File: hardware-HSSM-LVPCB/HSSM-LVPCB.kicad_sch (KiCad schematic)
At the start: 57 parts, among them J1 UFL_R_SMT_1_10, J2 LPPB061NGCN-RC, Q1 Q_MOSFET_N_BSS123, Q2 Q_MOSFET_N_BSS123, U1 ESP32-C6, U2 W25Q64JVSSIQ_SOIC-8, X1 X_40MHz_SMD_ECS-2520SMV-400-F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

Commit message: [#13] PCB routing WIP GPIO
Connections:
- net GPIO_Q2: now also U1.16 (GPIO10); no longer U1.6 (XTAL_32K_P)
- net GPIO_S2: now also U1.18 (GPIO12); no longer U1.17 (GPIO11)
- net GPIO_S3: now also U1.17 (GPIO11)
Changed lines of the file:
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@@
-	(wire
-		(pts
-			(xy 93.98 121.92) (xy 104.14 121.92)
-		)
-		(stroke
-			(width 0)
-			(type default)
-		)
-	)
 	(wire
 		(pts
@@
 	(wire
 		(pts
+			(xy 152.4 165.1) (xy 152.4 154.94)
+		)
+		(stroke
+			(width 0)
+			(type default)
+		)
+	)
+	(wire
+		(pts
 			(xy 193.04 54.61) (xy 191.77 54.61)
 		)
@@
 	(wire
 		(pts
+			(xy 142.24 165.1) (xy 142.24 154.94)
+		)
+		(stroke
+			(width 0)
+			(type default)
+		)
+	)
+	(wire
+		(pts
 			(xy 180.34 50.8) (xy 193.04 50.8)
 		)
@@
 	(wire
 		(pts
+			(xy 147.32 165.1) (xy 147.32 154.94)
+		)
+		(stroke
+			(width 0)
+			(type default)
+		)
+	)
+	(wire
+		(pts
 			(xy 152.4 83.82) (xy 152.4 77.47)
 		)
@@
 		(pts
 			(xy 280.67 219.71) (xy 290.83 219.71)
-		)
-		(stroke
-			(width 0)
-			(type default)
-		)
-	)
-	(wire
-		(pts
-			(xy 147.32 165.1) (xy 147.32 154.94)
 		)
 		(stroke
@@
 		)
 	)
-	(label "GPIO_S2"
-		(at 147.32 165.1 90)
-		(fields_autoplaced yes)
-		(effects
-			(font
-				(size 1.27 1.27)
-			)
-			(justify left bottom)
-		)
-	)
 	(label "GPIO_S3"
 		(at 187.96 68.58 0)
@@
 		)
 	)
-	(label "GPIO_Q2"
-		(at 93.98 121.92 0)
-		(fields_autoplaced yes)
-		(effects
-			(font
-				(size 1.27 1.27)
-			)
-			(justify left bottom)
-		)
-	)
 	(label "GPIO_Q1"
 		(at 162.56 73.66 270)
@@
 		)
 	)
+	(label "GPIO_S3"
+		(at 147.32 165.1 90)
+		(fields_autoplaced yes)
+		(effects
+			(font
+				(size 1.27 1.27)
+			)
+			(justify left bottom)
+		)
+	)
 	(label "S3_sym"
 		(at 95.25 132.08 0)
@@
 		)
 	)
+	(label "GPIO_Q2"
+		(at 142.24 165.1 90)
+		(fields_autoplaced yes)
+		(effects
+			(font
+				(size 1.27 1.27)
+			)
+			(justify left bottom)
+		)
+	)
 	(label "GPIO_S1"
 		(at 157.48 73.66 270)
@@
 		(fields_autoplaced yes)
 		(effects
+			(font
+				(size 1.27 1.27)
+			)
+			(justify left bottom)
+		)
+	)
+	(label "GPIO_S2"
+		(at 152.4 165.1 90)
+		(fields_autoplaced yes)
+		(effects

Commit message: Add additional signals to FCB between PCBs
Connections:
- net DEV_RX is gone; now on net LP_UART_TXD: CON1.8
- net DEV_TX is gone; now on net LP_UART_RXD: CON1.7
- net P_MEAS_RST: now reaches CON1.10
- net DO3: now reaches CON1.5
- net DO2: now reaches CON1.6
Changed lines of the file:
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@@
-	(wire
-		(pts
-			(xy 240.03 152.4) (xy 251.46 152.4)
-		)
-		(stroke
-			(width 0)
-			(type default)
-		)
-	)
 	(wire
 		(pts
@@
 	(wire
 		(pts
-			(xy 240.03 160.02) (xy 251.46 160.02)
+			(xy 228.6 160.02) (xy 251.46 160.02)
 		)
 		(stroke
@@
 	(wire
 		(pts
-			(xy 240.03 154.94) (xy 251.46 154.94)
-		)
-		(stroke
-			(width 0)
-			(type default)
-		)
-	)
-	(wire
-		(pts
-			(xy 240.03 147.32) (xy 251.46 147.32)
+			(xy 233.68 147.32) (xy 251.46 147.32)
 		)
 		(stroke
@@
 	(wire
 		(pts
-			(xy 187.96 73.66) (xy 198.12 73.66)
-		)
-		(stroke
-			(width 0)
-			(type default)
-		)
-	)
-	(wire
-		(pts
 			(xy 55.88 87.63) (xy 55.88 90.17)
 		)
@@
 	(wire
 		(pts
-			(xy 187.96 83.82) (xy 198.12 83.82)
-		)
-		(stroke
-			(width 0)
-			(type default)
-		)
-	)
-	(wire
-		(pts
 			(xy 128.27 176.53) (xy 132.08 176.53)
 		)
@@
 	(wire
 		(pts
-			(xy 187.96 68.58) (xy 198.12 68.58)
-		)
-		(stroke
-			(width 0)
-			(type default)
-		)
-	)
-	(wire
-		(pts
 			(xy 250.19 137.16) (xy 251.46 137.16)
 		)
@@
 	(wire
 		(pts
-			(xy 222.25 154.94) (xy 236.22 154.94)
+			(xy 237.49 152.4) (xy 251.46 152.4)
 		)
 		(stroke
@@
 	(wire
 		(pts
-			(xy 187.96 78.74) (xy 198.12 78.74)
-		)
-		(stroke
-			(width 0)
-			(type default)
-		)
-	)
-	(wire
-		(pts
 			(xy 271.78 219.71) (xy 280.67 219.71)
 		)
@@
 	(wire
 		(pts
-			(xy 240.03 149.86) (xy 251.46 149.86)
+			(xy 233.68 149.86) (xy 251.46 149.86)
 		)
 		(stroke
@@
 	(wire
 		(pts
+			(xy 146.05 177.8) (xy 168.91 177.8)
+		)
+		(stroke
+			(width 0)
+			(type default)
+		)
+	)
+	(wire
+		(pts
 			(xy 392.43 224.79) (xy 389.89 224.79)
 		)
@@
 	(wire
 		(pts
-			(xy 222.25 152.4) (xy 236.22 152.4)
+			(xy 237.49 154.94) (xy 251.46 154.94)
 		)
 		(stroke
@@
 		)
 	)
-	(label "GPIO23"
-		(at 187.96 83.82 0)
-		(fields_autoplaced yes)
-		(effects
-			(font
-				(size 1.27 1.27)
-			)
-			(justify left bottom)
-		)
-	)
 	(label "GPIO8"
 		(at 132.08 165.1 90)
@@
 		)
 	)
-	(label "DEV_TX"
-		(at 240.03 152.4 0)
-		(fields_autoplaced yes)
-		(effects
-			(font
-				(size 1.27 1.27)
-			)
-			(justify left bottom)
-		)
-	)
 	(label "S2_sym"
 		(at 93.98 127 0)
@@
 		)
 	)
+	(label "DO3"
+		(at 233.68 147.32 0)
+		(fields_autoplaced yes)
+		(effects
+			(font
+				(size 1.27 1.27)
+			)
+			(justify left bottom)
+		)
+	)
 	(label "SPICLK"
 		(at 204.47 121.92 180)
@@
 		)
 	)
-	(label "GPIO_S3"
-		(at 187.96 68.58 0)
-		(fields_autoplaced yes)
-		(effects
-			(font
-				(size 1.27 1.27)
-			)
-			(justify left bottom)
-		)
-	)
 	(label "LP_UART_TXD"
 		(at 116.84 168.91 90)
@@
 		)
 	)
+	(label "DO2"
+		(at 233.68 149.86 0)
+		(fields_autoplaced yes)
+		(effects
+			(font
+				(size 1.27 1.27)
+			)
+			(justify left bottom)
+		)
+	)
 	(label "SPIWP"
 		(at 204.47 137.16 180)
@@
 		)
 	)
-	(label "GPIO22"
-		(at 187.96 78.74 0)
-		(fields_autoplaced yes)
-		(effects
-			(font
-				(size 1.27 1.27)
-			)
-			(justify left bottom)
-		)
-	)
-	(label "DEV_RX"
-		(at 240.03 154.94 0)
+	(label "P_MEAS_RST"
+		(at 146.05 177.8 0)
 		(fields_autoplaced yes)
 		(effects
@@
 		)
 	)
-	(label "GPIO21"
-		(at 187.96 73.66 0)
-		(fields_autoplaced yes)
-		(effects
-			(font
-				(size 1.27 1.27)
-			)
-			(justify left bottom)
-		)
-	)
 	(label "LP_UART_RXD"
-		(at 222.25 154.94 0)
+		(at 237.49 152.4 0)
 		(fields_autoplaced yes)
 		(effects
@@
 		)
 	)
+	(label "P_MEAS_RST"
+		(at 228.6 160.02 0)
+		(fields_autoplaced yes)
+		(effects
+			(font
+				(size 1.27 1.27)
+			)
+			(justify left bottom)
+		)
+	)
 	(label "SPICLK"
 		(at 231.14 50.8 180)
@@
 	)
 	(label "LP_UART_TXD"
-		(at 222.25 152.4 0)
-		(fields_autoplaced yes)
-		(effects
+		(at 237.49 154.94 0)
+		(fields_autoplaced yes)
+		(effects

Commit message: [#13] PCB routing WIP prog signals
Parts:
- removed Q1, Q2: Q_MOSFET_N_BSS123, HSSM-LVPCB:SOT-23, symbol HSSM-LVPCB:Q_MOSFET_N_BSS123
- removed R10, R9: R_499R_1pct_0402_RC0402FR-07499RL, HSSM-LVPCB:R_0402, symbol HSSM-LVPCB:R_499R_1pct_0402_RC0402FR-07499RL
- removed R20, R21: R_10k_1pct_0402_RC0402FR-0710KL, HSSM-LVPCB:R_0402, symbol HSSM-LVPCB:R_10k_1pct_0402_RC0402FR-0710KL
- added C15, C20, C21: C_0u1_10pct_50V_0402_GRM155R71H104KE14D, HSSM-LVPCB:C_0402, symbol HSSM-LVPCB:C_0u1_10pct_50V_0402_GRM155R71H104KE14D
- added R23, R24: R_10k_1pct_0402_RC0402FR-0710KL, HSSM-LVPCB:R_0402, symbol HSSM-LVPCB:R_10k_1pct_0402_RC0402FR-0710KL
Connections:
- net DTR is gone; now on net BOOT: J2.2
- net RTS is gone; now on net Enable: J2.3
- net +3V3: now also R23.1, R24.1
- net BOOT: now also C20.2, R23.2
- net Enable: now also C15.2, R24.2
- net GND: now also C15.1, C20.1, C21.1
- net GPIO8: now also C21.2
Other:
- moved on the sheet: J2, R22

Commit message: [#13] PCB routing WIP GPIO
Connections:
- net S3_sym: now also U1.12 (MTCK); no longer U1.8 (GPIO2)
- no-connect marks 3 -> 2
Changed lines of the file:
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@@
 		(at 127 154.94)
 	)
-	(no_connect
-		(at 121.92 154.94)
-	)
 	(wire
 		(pts
@@
 	(wire
 		(pts
+			(xy 121.92 163.83) (xy 121.92 154.94)
+		)
+		(stroke
+			(width 0)
+			(type default)
+		)
+	)
+	(wire
+		(pts
 			(xy 336.55 212.09) (xy 336.55 217.17)
 		)
@@
 		(pts
 			(xy 351.79 217.17) (xy 351.79 212.09)
-		)
-		(stroke
-			(width 0)
-			(type default)
-		)
-	)
-	(wire
-		(pts
-			(xy 95.25 132.08) (xy 104.14 132.08)
 		)
 		(stroke
@@
 		)
 	)
+	(label "S3_sym"
+		(at 121.92 163.83 90)
+		(fields_autoplaced yes)
+		(effects
+			(font
+				(size 1.27 1.27)
+			)
+			(justify left bottom)
+		)
+	)
 	(label "BOOT"
 		(at 134.62 205.74 180)
@@
 		(fields_autoplaced yes)
 		(effects
-			(font
-				(size 1.27 1.27)
-			)
-			(justify left bottom)
-		)
-	)
-	(label "S3_sym"
-		(at 95.25 132.08 0)
-		(fields_autoplaced yes)
-		(effects

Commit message: [#13] PCB routing
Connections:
- net DO1: now also U1.13 (MTDO)
- net DO2: now also U1.6 (XTAL_32K_P)
- net DO3: now also U1.9 (GPIO3)
- net P_MEAS_RST: now also U1.27 (GPIO15)
- no-connect marks 2 -> 0
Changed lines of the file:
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@@
 		(color 0 0 0 0)
 	)
-	(no_connect
-		(at 175.26 111.76)
-	)
-	(no_connect
-		(at 127 154.94)
-	)
 	(wire
 		(pts
@@
 	(wire
 		(pts
+			(xy 90.17 137.16) (xy 104.14 137.16)
+		)
+		(stroke
+			(width 0)
+			(type default)
+		)
+	)
+	(wire
+		(pts
 			(xy 219.71 238.76) (xy 219.71 243.84)
 		)
@@
 	(wire
 		(pts
+			(xy 204.47 111.76) (xy 175.26 111.76)
+		)
+		(stroke
+			(width 0)
+			(type default)
+		)
+	)
+	(wire
+		(pts
 			(xy 50.8 81.28) (xy 55.88 81.28)
 		)
@@
 	(wire
 		(pts
+			(xy 127 165.1) (xy 127 154.94)
+		)
+		(stroke
+			(width 0)
+			(type default)
+		)
+	)
+	(wire
+		(pts
 			(xy 238.76 217.17) (xy 238.76 220.98)
 		)
@@
 	(wire
 		(pts
-			(xy 146.05 177.8) (xy 168.91 177.8)
-		)
-		(stroke
-			(width 0)
-			(type default)
-		)
-	)
-	(wire
-		(pts
 			(xy 392.43 224.79) (xy 389.89 224.79)
 		)
@@
 	(wire
 		(pts
+			(xy 93.98 121.92) (xy 104.14 121.92)
+		)
+		(stroke
+			(width 0)
+			(type default)
+		)
+	)
+	(wire
+		(pts
 			(xy 217.17 226.06) (xy 217.17 229.87)
 		)
@@
 		)
 	)
+	(label "DO2"
+		(at 93.98 121.92 0)
+		(fields_autoplaced yes)
+		(effects
+			(font
+				(size 1.27 1.27)
+			)
+			(justify left bottom)
+		)
+	)
 	(label "DO3"
 		(at 233.68 147.32 0)
@@
 		)
 	)
+	(label "DO1"
+		(at 127 165.1 90)
+		(fields_autoplaced yes)
+		(effects
+			(font
+				(size 1.27 1.27)
+			)
+			(justify left bottom)
+		)
+	)
 	(label "Enable"
 		(at 113.03 205.74 180)
@@
 		)
 	)
+	(label "DO3"
+		(at 90.17 137.16 0)
+		(fields_autoplaced yes)
+		(effects
+			(font
+				(size 1.27 1.27)
+			)
+			(justify left bottom)
+		)
+	)
 	(label "GPIO_Q2"
 		(at 233.68 170.18 0)
@@
 		)
 	)
+	(label "P_MEAS_RST"
+		(at 204.47 111.76 180)
+		(fields_autoplaced yes)
+		(effects
+			(font
+				(size 1.27 1.27)
+			)
+			(justify right bottom)
+		)
+	)
 	(label "LP_UART_RXD"
 		(at 90.17 142.24 0)
@@
 		)
 	)
-	(label "P_MEAS_RST"
-		(at 146.05 177.8 0)
-		(fields_autoplaced yes)
-		(effects
-			(font
-				(size 1.27 1.27)
-			)
-			(justify left bottom)
-		)
-	)
 	(label "U0TXD"
 		(at 207.01 101.6 180)
@@
 		(on_board yes)
 		(dnp no)
-		(fields_autoplaced yes)
 		(property "Reference" "U1"
 			(at 179.07 90.2015 0)

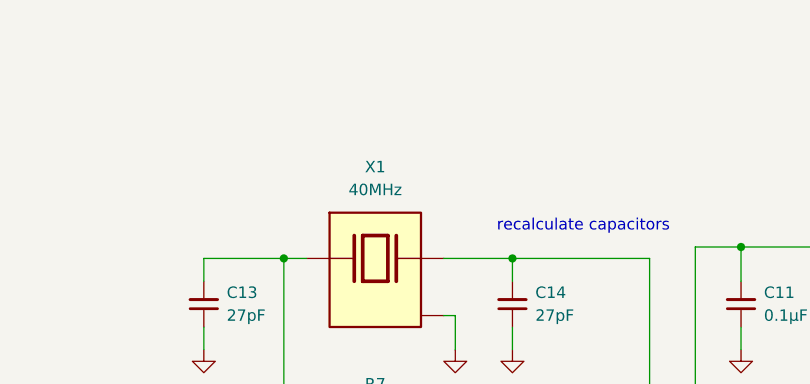
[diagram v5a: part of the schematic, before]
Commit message: [#13] Add oscillator CN4040M00010001
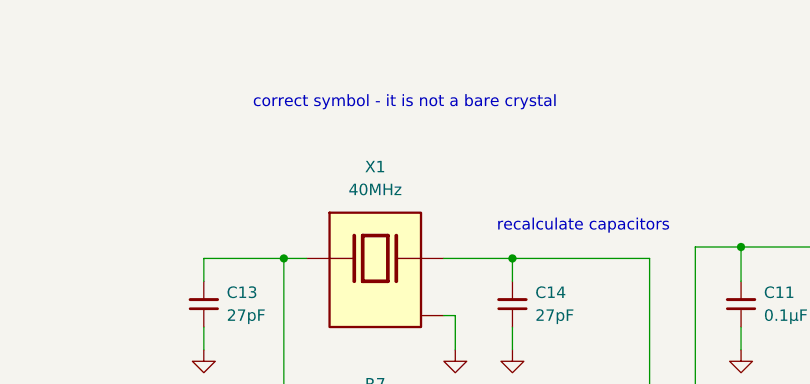
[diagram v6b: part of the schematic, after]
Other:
- note added: "correct symbol - it is not a bare crystal"
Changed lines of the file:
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@@
+		)
+	)
+	(text "correct symbol - it is not a bare crystal"
+		(exclude_from_sim no)
+		(at 99.822 32.258 0)
+		(effects
+			(font
+				(size 1.27 1.27)
+			)
 		)
 	)

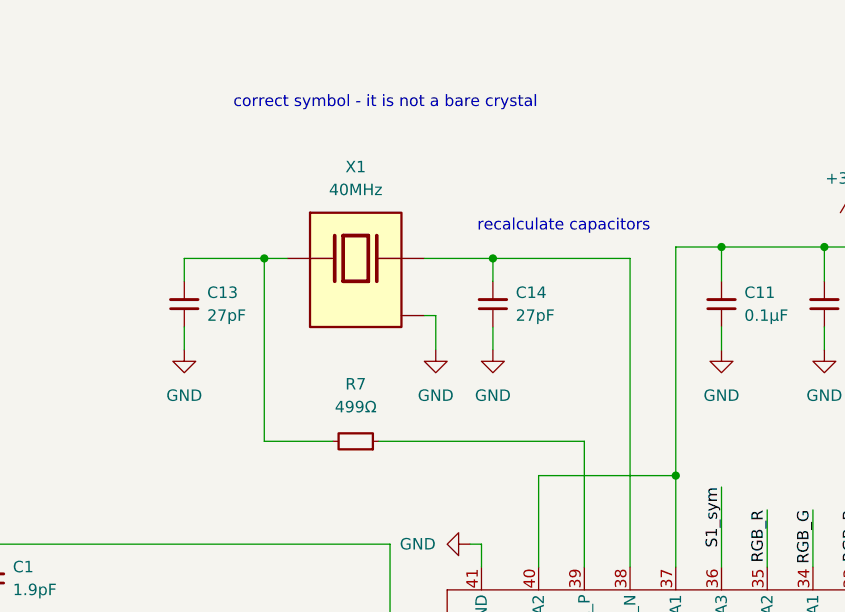
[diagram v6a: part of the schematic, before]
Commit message: [#13] Correct crystal
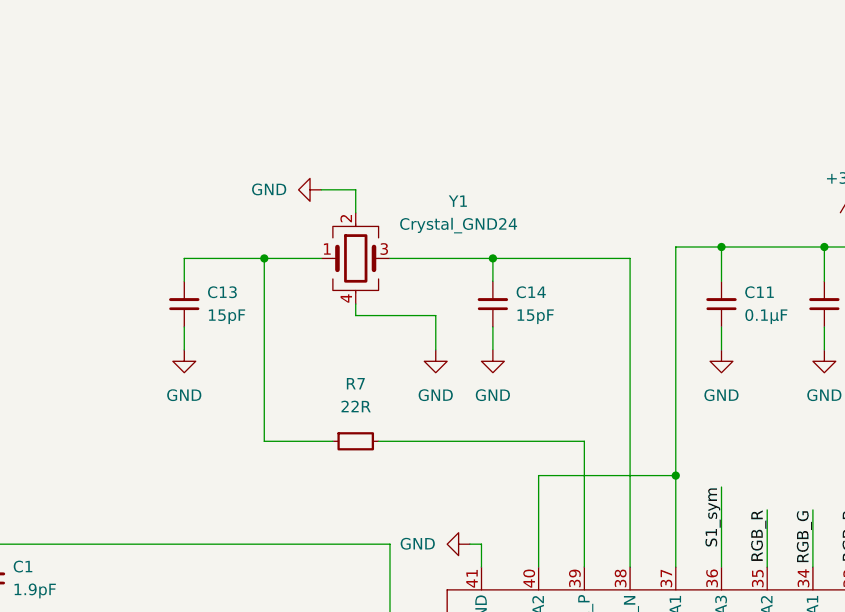
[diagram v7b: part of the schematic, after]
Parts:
- removed C13, C14: C_27pF_5pct_50V_0402_GCM1555C1H270JA16J, HSSM-LVPCB:C_0402, symbol HSSM-LVPCB:C_27pF_5pct_50V_0402_GCM1555C1H270JA16J
- removed R7: R_499R_1pct_0402_RC0402FR-07499RL, HSSM-LVPCB:R_0402, symbol HSSM-LVPCB:R_499R_1pct_0402_RC0402FR-07499RL
- removed X1: X_40MHz_SMD_ECS-2520SMV-400-FN-TR, HSSM-LVPCB:ECS-2520SMV-400-FN-TR, symbol HSSM-LVPCB:X_40MHz_SMD_ECS-2520SMV-400-FN-TR
- added C13, C14: C_15pF_1pct_50V_0402_C0402C150F5GACAUTO, HSSM-LVPCB:C_0402, symbol HSSM-LVPCB:C_15pF_1pct_50V_0402_C0402C150F5GACAUTO
- added R7: R_22R_1pct_0402_CRCW040222R0FKED, HSSM-LVPCB:R_0402, symbol HSSM-LVPCB:R_22R_1pct_0402_CRCW040222R0FKED
- added Y1: Crystal_GND24, HSSM-LVPCB:Crystal_SMD_2016-4Pin_2.0x1.6mm, symbol HSSM-LVPCB:Crystal_GND24
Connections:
- net GND: now also C13.1, C14.1, Y1.2, Y1.4
- net at U1.39 (XTAL_P): now also R7.2
- net at U1.38 (XTAL_N): now also C14.2, Y1.3
- new net: C13.2, R7.1, Y1.1
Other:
- note removed: "correct symbol - it is not a bare crystal"
- note removed: "recalculate capacitors"

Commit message: [#13] PCB generate gerber files
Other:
- title: (none) -> HSSM-LVPCB
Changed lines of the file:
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@@
 	(generator_version "8.0")
 	(paper "A3")
+	(title_block
+		(title "HSSM-LVPCB")
+		(date "2025-01-21")
+		(rev "1.0.0")
+	)
 	(junction
 		(at 384.81 228.6)
